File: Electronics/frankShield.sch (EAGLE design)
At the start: 24 parts, among them IC1 BD6230F, IC2 BD6230F, IC3 TS5A23157

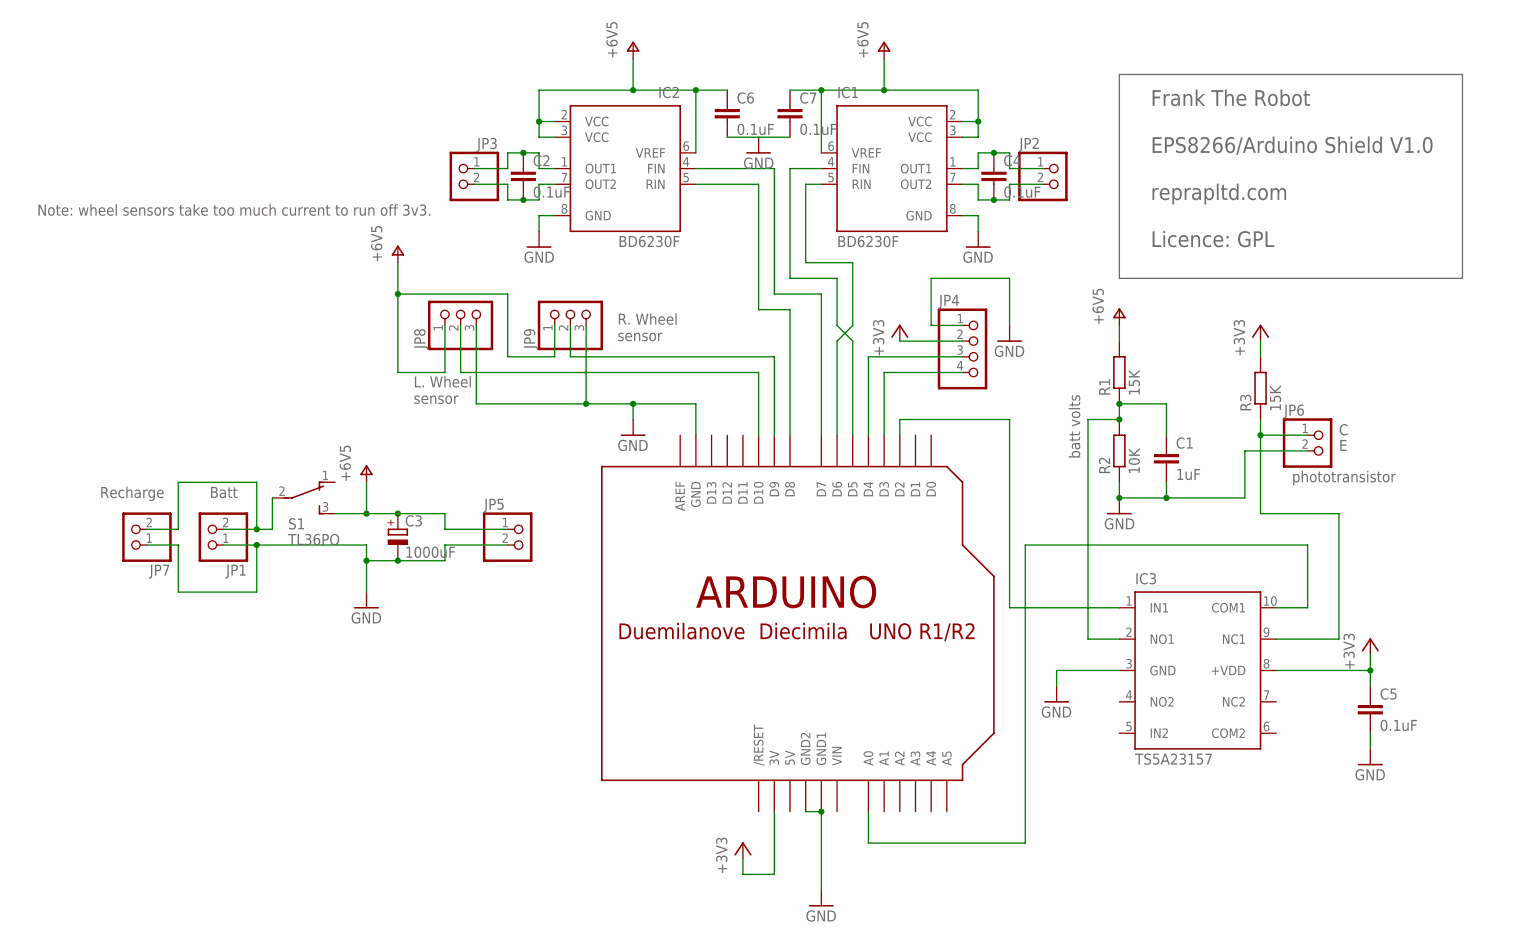
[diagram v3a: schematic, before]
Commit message: Added LED to shield, and anti-short safety diode to the charge circuit.
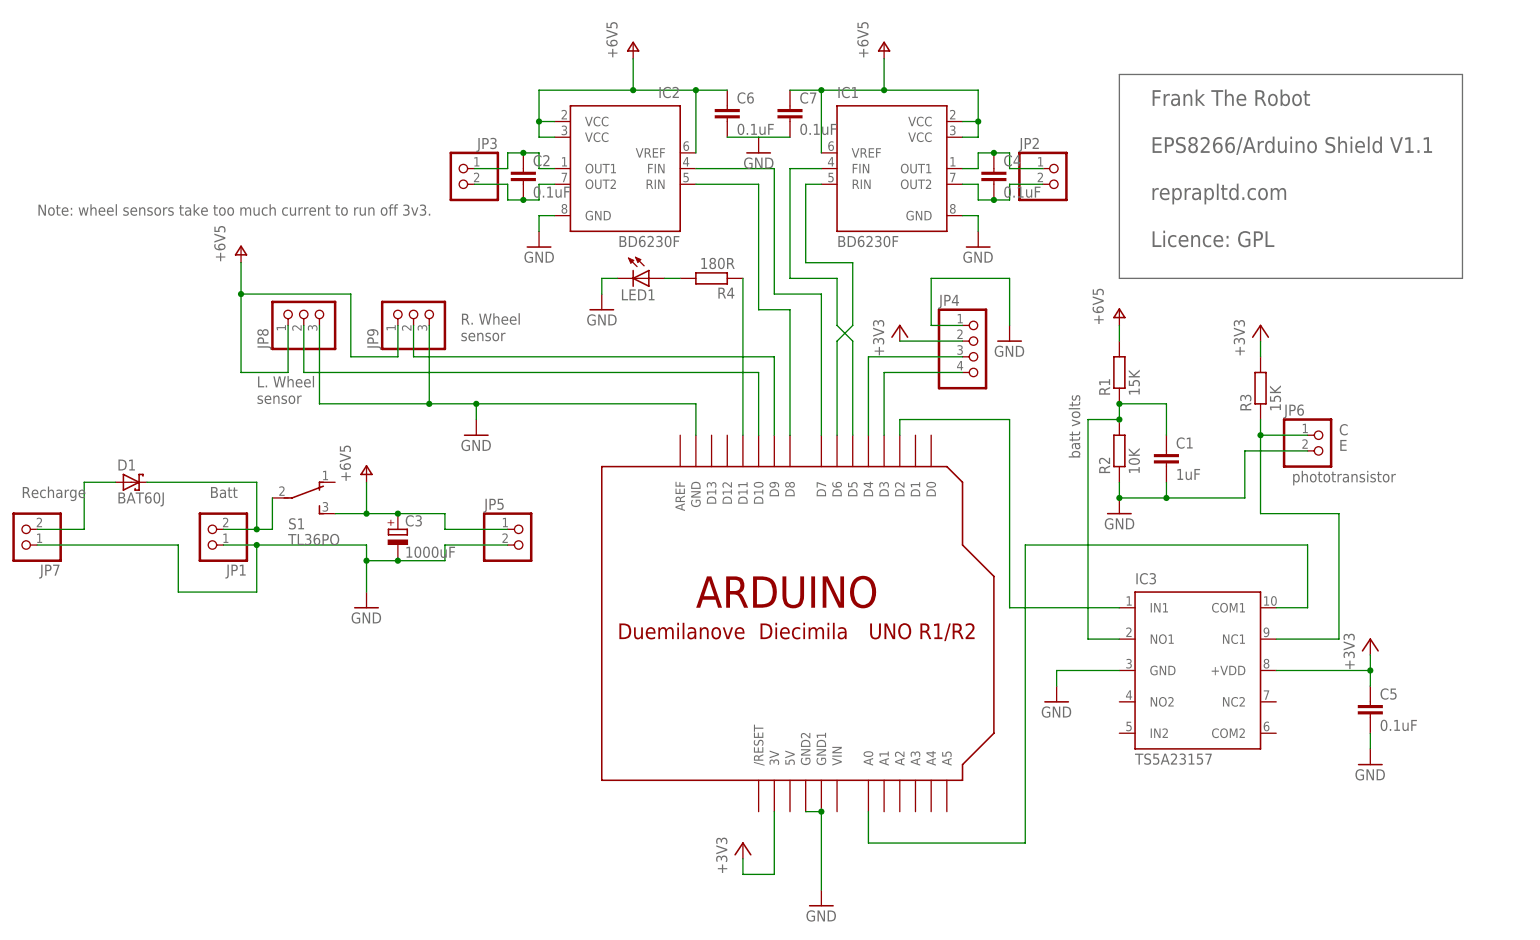
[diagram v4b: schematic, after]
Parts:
- added D1: BAT60J, diode:BAT60J
- added LED1: (no value), led:LEDCHIP-LED0805
- added R4: 180R, rcl:R-EU_M0805
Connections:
- new net N$16: D1.A, JP7.2
- new net N$19: LED1.A, R4.2
- new net N$20: R4.1, U$1.D11
- net GND: now also LED1.C
- net N$13: now also D1.C; no longer JP7.2
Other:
- note added: "Frank The Robot EPS8266/Arduino Shield V1.1 reprapltd.com Licence: GPL"
- note removed: "Frank The Robot EPS8266/Arduino Shield V1.0 reprapltd.com Licence: GPL"
- moved on the sheet: JP7, JP8, JP9
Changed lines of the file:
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@@
 <part name="GND10" library="supply1" deviceset="GND" device=""/>
 <part name="P+5" library="supply1" deviceset="V+" device="" value="+6V5"/>
+<part name="D1" library="diode" deviceset="BAT60J" device=""/>
+<part name="LED1" library="led" deviceset="LED" device="CHIP-LED0805"/>
+<part name="GND11" library="supply1" deviceset="GND" device=""/>
+<part name="R4" library="rcl" deviceset="R-EU_" device="M0805" value="180R"/>
 </parts>
 <sheets>
@@
 <text x="132.08" y="76.2" size="1.778" layer="95">E</text>
 <text x="101.6" y="109.22" size="2.54" layer="95">Frank The Robot
-EPS8266/Arduino Shield V1.0
+EPS8266/Arduino Shield V1.1
 reprapltd.com
 Licence: GPL</text>
@@
 <wire x1="96.52" y1="137.16" x2="96.52" y2="104.14" width="0.1524" layer="95"/>
 <text x="-50.8" y="68.58" size="1.778" layer="95">Batt</text>
-<text x="-68.58" y="68.58" size="1.778" layer="96">Recharge</text>
-<text x="-17.78" y="83.82" size="1.778" layer="96">L. Wheel
+<text x="-81.28" y="68.58" size="1.778" layer="96">Recharge</text>
+<text x="-43.18" y="83.82" size="1.778" layer="96">L. Wheel
 sensor</text>
-<text x="15.24" y="93.98" size="1.778" layer="96">R. Wheel
+<text x="-10.16" y="93.98" size="1.778" layer="96">R. Wheel
 sensor</text>
 <text x="90.17" y="74.93" size="1.778" layer="96" rot="R90">batt volts</text>
@@
 <instance part="C1" gate="G$1" x="104.14" y="76.2"/>
 <instance part="S1" gate="BEF1" x="-35.56" y="68.58" rot="R270"/>
-<instance part="GND8" gate="1" x="17.78" y="78.74"/>
-<instance part="JP7" gate="G$1" x="-63.5" y="63.5" rot="R180"/>
-<instance part="JP8" gate="A" x="-10.16" y="99.06" rot="R90"/>
-<instance part="JP9" gate="A" x="7.62" y="99.06" rot="R90"/>
+<instance part="GND8" gate="1" x="-7.62" y="78.74"/>
+<instance part="JP7" gate="G$1" x="-81.28" y="63.5" rot="R180"/>
+<instance part="JP8" gate="A" x="-35.56" y="99.06" rot="R90"/>
+<instance part="JP9" gate="A" x="-17.78" y="99.06" rot="R90"/>
 <instance part="C2" gate="G$1" x="0" y="121.92"/>
 <instance part="C4" gate="G$1" x="76.2" y="121.92"/>
@@
 <instance part="C7" gate="G$1" x="43.18" y="132.08"/>
 <instance part="GND10" gate="1" x="38.1" y="124.46" rot="MR0"/>
-<instance part="P+5" gate="1" x="-20.32" y="109.22"/>
+<instance part="P+5" gate="1" x="-45.72" y="109.22"/>
+<instance part="D1" gate="G$1" x="-63.5" y="71.12"/>
+<instance part="LED1" gate="G$1" x="20.32" y="104.14" rot="R270"/>
+<instance part="GND11" gate="1" x="12.7" y="99.06" rot="MR0"/>
+<instance part="R4" gate="G$1" x="30.48" y="104.14" rot="R180"/>
 </instances>
 <busses>
@@
 <wire x1="-55.88" y1="53.34" x2="-55.88" y2="60.96" width="0.1524" layer="91"/>
 <pinref part="JP7" gate="G$1" pin="1"/>
-<wire x1="-55.88" y1="60.96" x2="-60.96" y2="60.96" width="0.1524" layer="91"/>
+<wire x1="-55.88" y1="60.96" x2="-78.74" y2="60.96" width="0.1524" layer="91"/>
 <junction x="-43.18" y="60.96"/>
 </segment>
@@
 <pinref part="U$1" gate="G$1" pin="GND"/>
 <wire x1="27.94" y1="78.74" x2="27.94" y2="83.82" width="0.1524" layer="91"/>
-<wire x1="27.94" y1="83.82" x2="17.78" y2="83.82" width="0.1524" layer="91"/>
+<wire x1="27.94" y1="83.82" x2="-7.62" y2="83.82" width="0.1524" layer="91"/>
 <pinref part="GND8" gate="1" pin="GND"/>
-<wire x1="17.78" y1="83.82" x2="17.78" y2="81.28" width="0.1524" layer="91"/>
-<wire x1="17.78" y1="83.82" x2="10.16" y2="83.82" width="0.1524" layer="91"/>
+<wire x1="-7.62" y1="83.82" x2="-7.62" y2="81.28" width="0.1524" layer="91"/>
+<wire x1="-7.62" y1="83.82" x2="-15.24" y2="83.82" width="0.1524" layer="91"/>
 <pinref part="JP9" gate="A" pin="3"/>
-<wire x1="10.16" y1="83.82" x2="10.16" y2="96.52" width="0.1524" layer="91"/>
+<wire x1="-15.24" y1="83.82" x2="-15.24" y2="96.52" width="0.1524" layer="91"/>
 <pinref part="JP8" gate="A" pin="3"/>
-<wire x1="10.16" y1="83.82" x2="-7.62" y2="83.82" width="0.1524" layer="91"/>
-<wire x1="-7.62" y1="83.82" x2="-7.62" y2="96.52" width="0.1524" layer="91"/>
-<junction x="17.78" y="83.82"/>
-<junction x="10.16" y="83.82"/>
+<wire x1="-15.24" y1="83.82" x2="-33.02" y2="83.82" width="0.1524" layer="91"/>
+<wire x1="-33.02" y1="83.82" x2="-33.02" y2="96.52" width="0.1524" layer="91"/>
+<junction x="-7.62" y="83.82"/>
+<junction x="-15.24" y="83.82"/>
 </segment>
 <segment>
@@
 <pinref part="C7" gate="G$1" pin="2"/>
 <wire x1="38.1" y1="127" x2="43.18" y2="127" width="0.1524" layer="91"/>
+</segment>
+<segment>
+<pinref part="LED1" gate="G$1" pin="C"/>
+<pinref part="GND11" gate="1" pin="GND"/>
+<wire x1="15.24" y1="104.14" x2="12.7" y2="104.14" width="0.1524" layer="91"/>
+<wire x1="12.7" y1="104.14" x2="12.7" y2="101.6" width="0.1524" layer="91"/>
 </segment>
 </net>
@@
 <segment>
 <pinref part="JP8" gate="A" pin="1"/>
-<wire x1="-12.7" y1="96.52" x2="-12.7" y2="88.9" width="0.1524" layer="91"/>
-<wire x1="-12.7" y1="88.9" x2="-20.32" y2="88.9" width="0.1524" layer="91"/>
-<wire x1="-20.32" y1="88.9" x2="-20.32" y2="101.6" width="0.1524" layer="91"/>
-<wire x1="-20.32" y1="101.6" x2="-2.54" y2="101.6" width="0.1524" layer="91"/>
-<wire x1="-2.54" y1="101.6" x2="-2.54" y2="91.44" width="0.1524" layer="91"/>
-<wire x1="-2.54" y1="91.44" x2="5.08" y2="91.44" width="0.1524" layer="91"/>
+<wire x1="-38.1" y1="96.52" x2="-38.1" y2="88.9" width="0.1524" layer="91"/>
+<wire x1="-38.1" y1="88.9" x2="-45.72" y2="88.9" width="0.1524" layer="91"/>
+<wire x1="-45.72" y1="88.9" x2="-45.72" y2="101.6" width="0.1524" layer="91"/>
+<wire x1="-45.72" y1="101.6" x2="-27.94" y2="101.6" width="0.1524" layer="91"/>
+<wire x1="-27.94" y1="101.6" x2="-27.94" y2="91.44" width="0.1524" layer="91"/>
+<wire x1="-27.94" y1="91.44" x2="-20.32" y2="91.44" width="0.1524" layer="91"/>
 <pinref part="JP9" gate="A" pin="1"/>
-<wire x1="5.08" y1="91.44" x2="5.08" y2="96.52" width="0.1524" layer="91"/>
-<junction x="-20.32" y="101.6"/>
+<wire x1="-20.32" y1="91.44" x2="-20.32" y2="96.52" width="0.1524" layer="91"/>
+<junction x="-45.72" y="101.6"/>
 <pinref part="P+5" gate="1" pin="V+"/>
-<wire x1="-20.32" y1="101.6" x2="-20.32" y2="106.68" width="0.1524" layer="91"/>
+<wire x1="-45.72" y1="101.6" x2="-45.72" y2="106.68" width="0.1524" layer="91"/>
 </segment>
 </net>
@@
 <pinref part="JP1" gate="G$1" pin="2"/>
 <wire x1="-43.18" y1="63.5" x2="-43.18" y2="71.12" width="0.1524" layer="91"/>
-<wire x1="-43.18" y1="71.12" x2="-55.88" y2="71.12" width="0.1524" layer="91"/>
-<wire x1="-55.88" y1="71.12" x2="-55.88" y2="63.5" width="0.1524" layer="91"/>
-<pinref part="JP7" gate="G$1" pin="2"/>
-<wire x1="-55.88" y1="63.5" x2="-60.96" y2="63.5" width="0.1524" layer="91"/>
+<wire x1="-43.18" y1="71.12" x2="-60.96" y2="71.12" width="0.1524" layer="91"/>
 <junction x="-43.18" y="63.5"/>
+<pinref part="D1" gate="G$1" pin="C"/>
 </segment>
 </net>
@@
 <pinref part="U$1" gate="G$1" pin="D9"/>
 <wire x1="40.64" y1="78.74" x2="40.64" y2="91.44" width="0.1524" layer="91"/>
-<wire x1="40.64" y1="91.44" x2="7.62" y2="91.44" width="0.1524" layer="91"/>
+<wire x1="40.64" y1="91.44" x2="-17.78" y2="91.44" width="0.1524" layer="91"/>
 <pinref part="JP9" gate="A" pin="2"/>
-<wire x1="7.62" y1="91.44" x2="7.62" y2="96.52" width="0.1524" layer="91"/>
+<wire x1="-17.78" y1="91.44" x2="-17.78" y2="96.52" width="0.1524" layer="91"/>
 </segment>
 </net>
@@
 <wire x1="38.1" y1="78.74" x2="38.1" y2="88.9" width="0.1524" layer="91"/>
 <pinref part="JP8" gate="A" pin="2"/>
-<wire x1="38.1" y1="88.9" x2="-10.16" y2="88.9" width="0.1524" layer="91"/>
-<wire x1="-10.16" y1="88.9" x2="-10.16" y2="96.52" width="0.1524" layer="91"/>
+<wire x1="38.1" y1="88.9" x2="-35.56" y2="88.9" width="0.1524" layer="91"/>
+<wire x1="-35.56" y1="88.9" x2="-35.56" y2="96.52" width="0.1524" layer="91"/>
 </segment>
 </net>
@@
 </segment>
 </net>
+<net name="N$16" class="0">
+<segment>
+<pinref part="JP7" gate="G$1" pin="2"/>
+<wire x1="-78.74" y1="63.5" x2="-71.12" y2="63.5" width="0.1524" layer="91"/>
+<wire x1="-71.12" y1="63.5" x2="-71.12" y2="71.12" width="0.1524" layer="91"/>
+<pinref part="D1" gate="G$1" pin="A"/>
+<wire x1="-71.12" y1="71.12" x2="-66.04" y2="71.12" width="0.1524" layer="91"/>
+</segment>
+</net>
+<net name="N$19" class="0">
+<segment>
+<pinref part="R4" gate="G$1" pin="2"/>
+<pinref part="LED1" gate="G$1" pin="A"/>
+<wire x1="25.4" y1="104.14" x2="22.86" y2="104.14" width="0.1524" layer="91"/>
+</segment>
+</net>
+<net name="N$20" class="0">
+<segment>
+<pinref part="R4" gate="G$1" pin="1"/>
+<pinref part="U$1" gate="G$1" pin="D11"/>
+<wire x1="35.56" y1="104.14" x2="35.56" y2="78.74" width="0.1524" layer="91"/>
+</segment>
+</net>
